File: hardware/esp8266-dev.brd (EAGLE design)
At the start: 48.3 x 48.3 mm, 19 parts, among them CON1 USBB-SOCKET, IC1 TBD, J1 AVR_SPI_PRG_6PTH

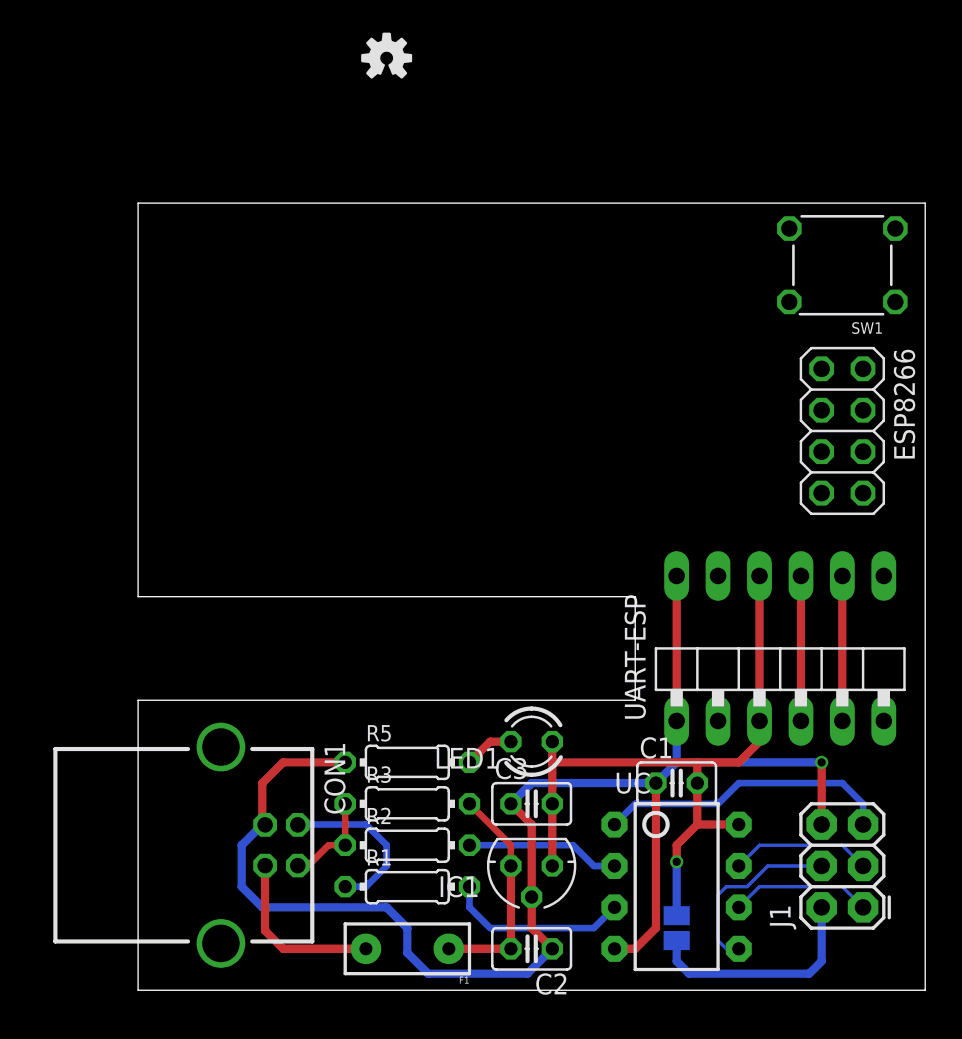
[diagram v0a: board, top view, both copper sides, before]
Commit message: Added ESP sub board with proto area
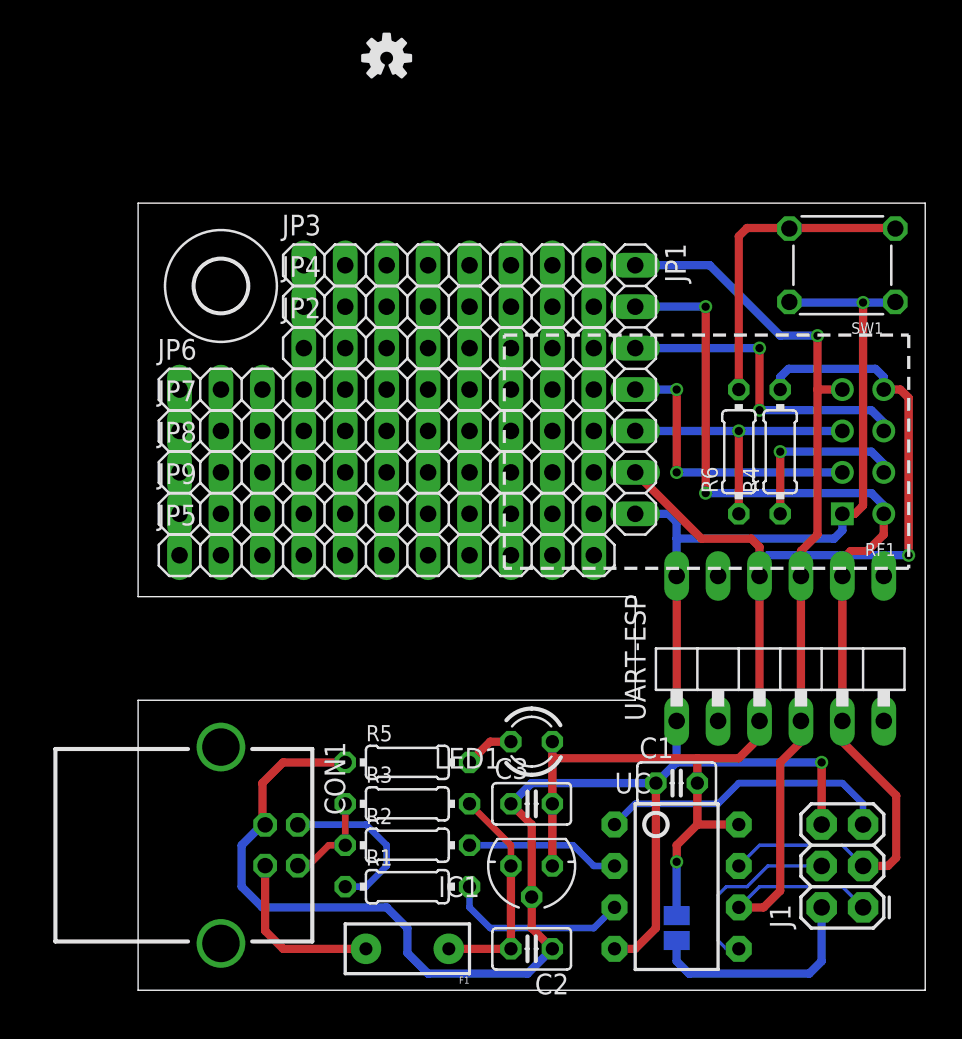
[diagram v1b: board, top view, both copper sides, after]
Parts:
- removed ESP8266: (no value), pinhead:2X04
- added H1: MOUNT-HOLE3.2, holes:3,2
- added JP1: (no value), pinhead:1X07
- added JP2, JP3, JP4: (no value), pinhead:1X08
- added JP5, JP6, JP7, JP8, JP9: (no value), pinhead:1X11
- added R4, R6: 10k, rcl:0204/7
- added RF1: ESP2866-ESP-01THT, p.peter-periphery:ESP8266-ESP-01
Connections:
- removed net N$7: UART-AVR.4, UART-ESP.4
- removed net PIN1: J1.1, UC.6
- removed net PIN2: J1.3, UC.7
- new net AVR-RX: J1.3, JP1.2, RF1.TX, UART-AVR.5, UART-ESP.5, UC.7
- new net AVR-TX: J1.1, JP1.1, RF1.RX, UART-AVR.4, UART-ESP.4, UC.6
- new net IO0: JP1.5, R6.1, RF1.GPIO0
- new net IO16: JP1.3, RF1.GPIO16
- new net IO2: JP1.4, RF1.GPIO2
- new net N$8: R6.2, SW1.P$1, SW1.P$2
- net +3V3: now also JP1.6, R4.2, RF1.VCC
- net GND: now also JP1.7, RF1.GND, SW1.P$3, SW1.P$4
- net N$6: now also R4.1, RF1.H_PD; no longer UART-AVR.5, UART-ESP.5
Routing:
- net AVR-RX: track 0.00 -> 62.5 mm, vias 0 -> 2
- net AVR-TX: track 0.00 -> 61.1 mm, vias 0 -> 1
- net +3V3: track 43.5 -> 84.6 mm, vias 1 -> 2
- net GND: track 92.8 -> 130.8 mm, vias 1 -> 2
- net IO16: track 0.00 -> 19.9 mm, vias 0 -> 2
- net N$8: track 0.00 -> 19.3 mm
- net IO0: track 0.00 -> 17.8 mm, vias 0 -> 1
- net IO2: track 0.00 -> 17.8 mm, vias 0 -> 2
- net N$7: track 8.89 -> 0.00 mm
- net PIN1: track 8.67 -> 0.00 mm
- net PIN2: track 8.67 -> 0.00 mm
- net N$6: track 8.89 -> 11.0 mm, vias 0 -> 1

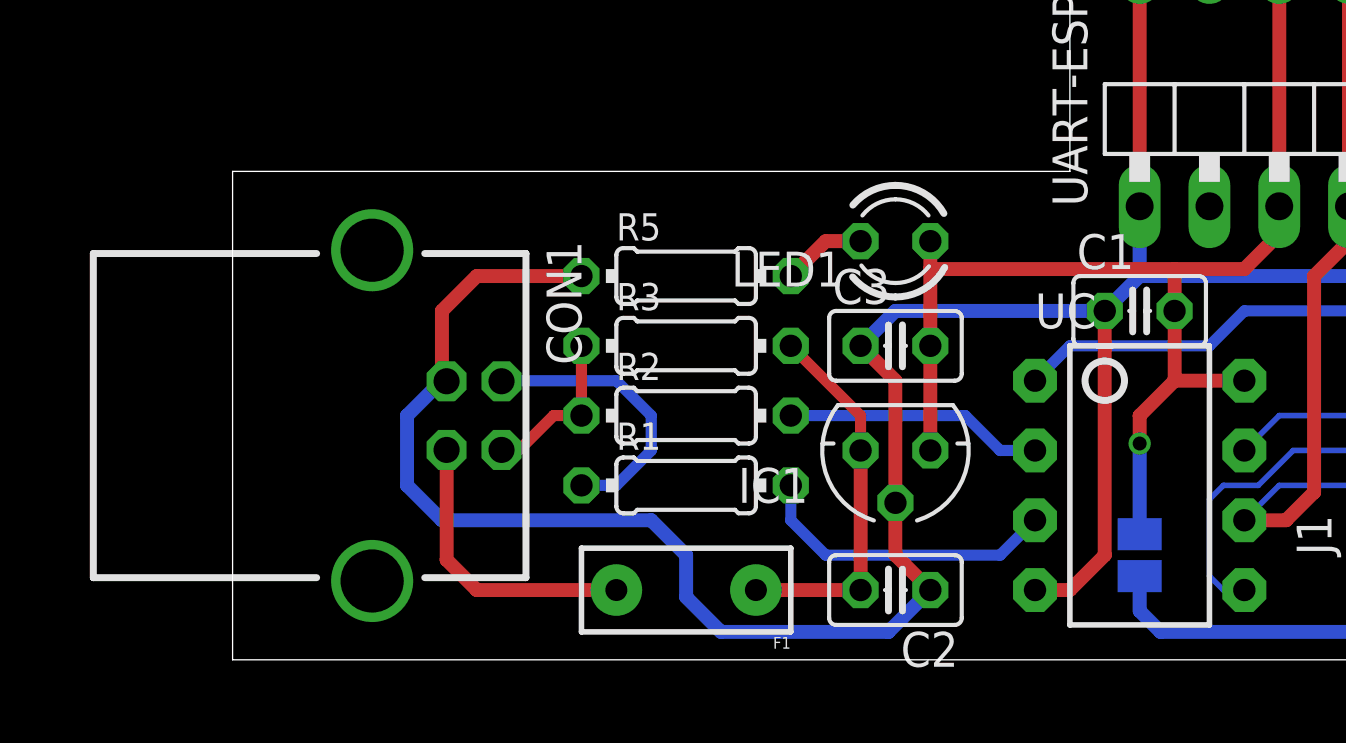
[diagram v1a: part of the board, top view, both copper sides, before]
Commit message: changed regulator to 500m suitable version and fuse to smaller footprint
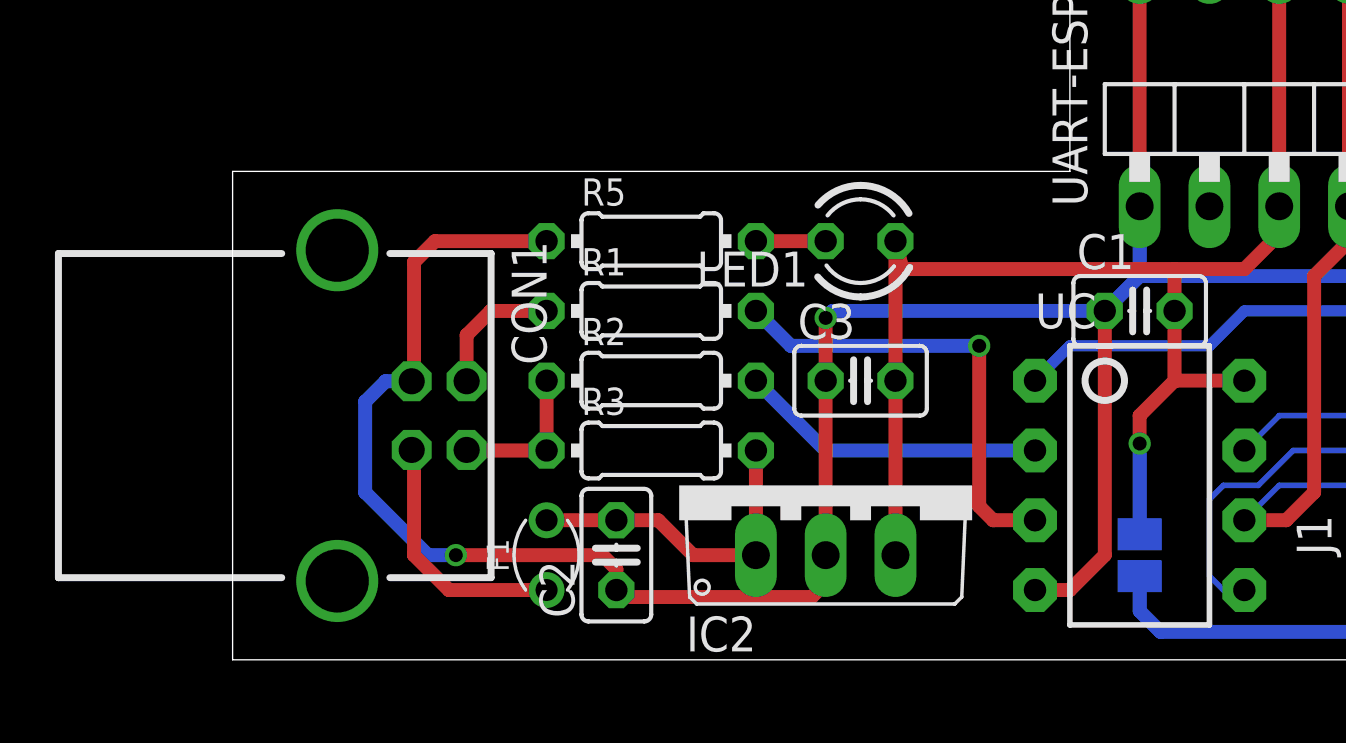
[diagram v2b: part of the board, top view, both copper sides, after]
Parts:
- removed IC1: TBD, v-reg:78LXX
- added IC2: (no value), p.peter-regulators:TO220V
- C2: value 100n -> 330n
- F1: value PTCPTH -> 500m; device SparkFun:PTC -> p.peter-regulators:FUSE-THT-100-MIL
- moved C2 10.2 mm to (14.0, 5.08), turned to 90 degrees
- moved R1 6.48 mm to (15.2, 14.0)
- moved F1 5.24 mm to (11.4, 5.08), turned to 90 degrees
- moved R3 4.02 mm to (15.2, 8.89)
- moved R5 1.80 mm to (15.2, 16.5)
- moved R2 1.80 mm to (15.2, 11.4)
- moved C3 1.80 mm to (22.9, 11.4)
- moved CON1 1.27 mm to (3.81, 10.2)
- moved LED1 1.27 mm to (22.9, 16.5)
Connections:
- net +3V3: now also IC2.3; no longer IC1.OUT
- net +5V: now also F1.P$2, IC2.1; no longer F1.P$1, IC1.IN
- net GND: now also IC2.2; no longer IC1.GND
- net N$4: now also F1.P$1; no longer F1.P$2
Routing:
- net +3V3: track 84.6 -> 90.4 mm
- net N$2: track 11.2 -> 16.7 mm, vias 0 -> 1
- net D+: track 10.4 -> 4.96 mm
- net N$1: track 9.42 -> 11.2 mm
- net +5V: track 13.8 -> 12.0 mm
- net N$4: track 10.6 -> 9.25 mm
- net GND: track 130.8 -> 129.6 mm, vias 2 -> 4
- net N$3: track 3.07 -> 2.54 mm

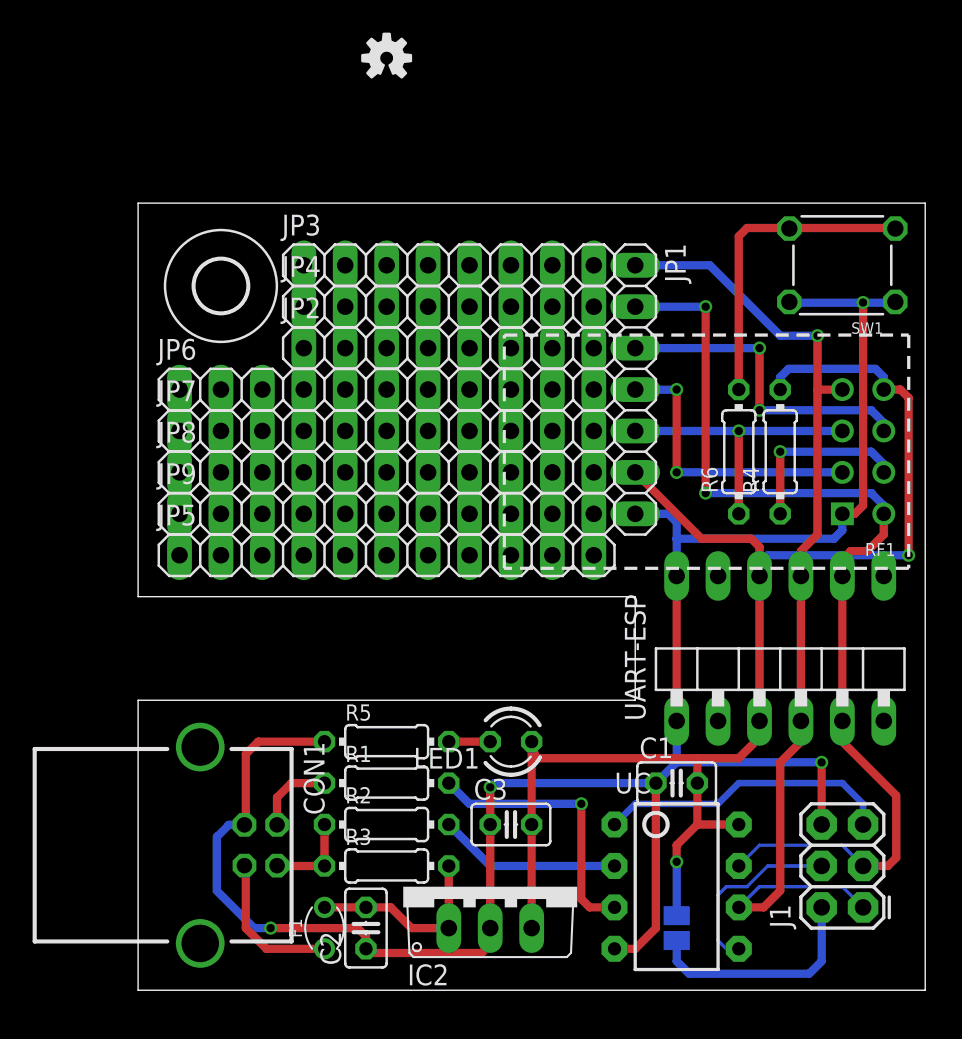
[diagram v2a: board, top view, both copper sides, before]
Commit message: basic lazyout done, cleaning up silkscreen
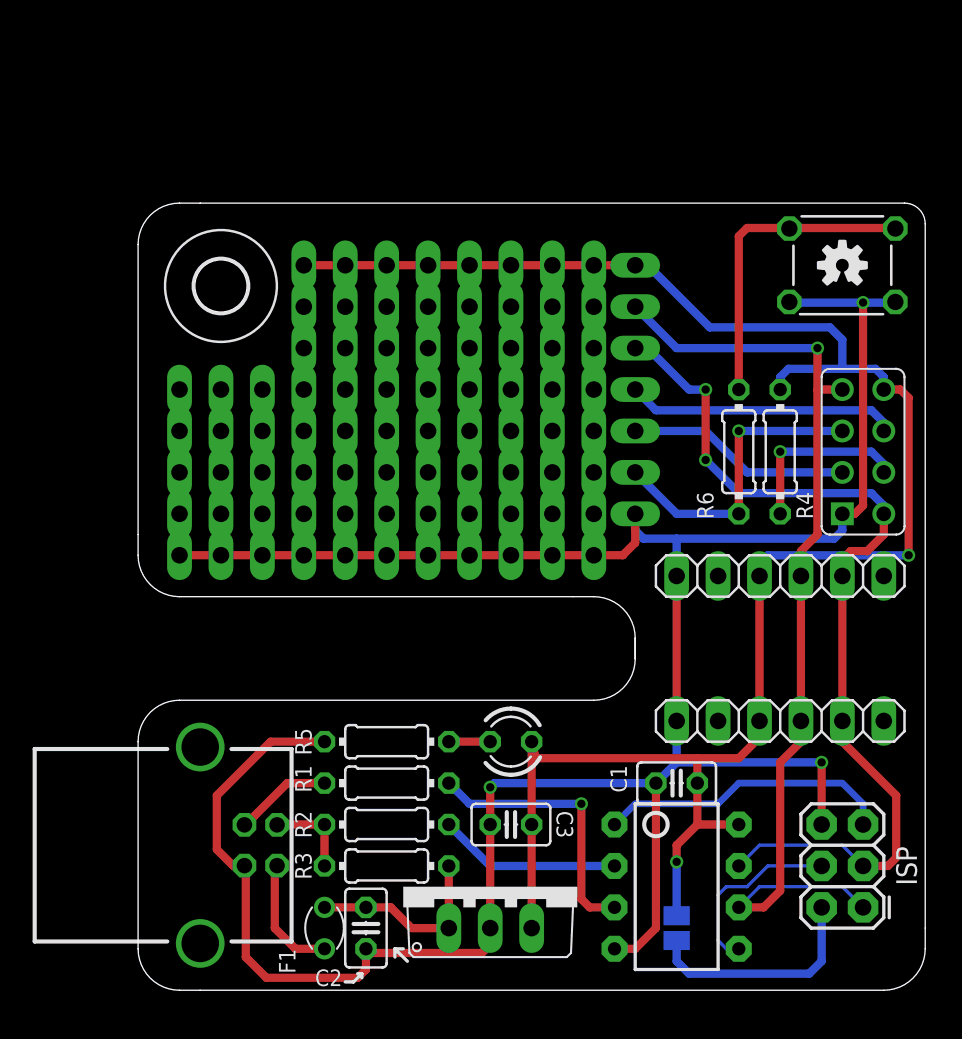
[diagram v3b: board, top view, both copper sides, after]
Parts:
- removed JP1: (no value), pinhead:1X07
- removed JP2, JP3, JP4: (no value), pinhead:1X08
- removed JP5, JP6, JP7, JP8, JP9: (no value), pinhead:1X11
- removed UART-AVR, UART-ESP: UART-6_PIN, p.peter-connectors:ANGLE-1X6
- added AVR-UART, ESP-UART: (no value), p.peter-connectors:PINHEADER-100MIL-1X6
- added CON10: (no value), p.peter-connectors:PINHEADER-100MIL-1X7-NOSILK
- added CON2, CON3, CON4: (no value), p.peter-connectors:PINHEADER-100MIL-1X8-NOSILK
- added CON5, CON6, CON7, CON8, CON9: (no value), p.peter-connectors:PINHEADER-100MIL-1X11-NOSILK
- RF1: value ESP2866-ESP-01THT -> (none); device p.peter-periphery:ESP8266-ESP-01 -> p.peter-periphery:ESP8266-ESP-01-NOSILK
- UC: value ATTINY45DIP8 -> ATTINY85
- moved U$1 30.7 mm to (43.2, 45.7)
- renumbered J1 to ISP
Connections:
- removed net N$5: CON1.D-, R2.1, R3.1
- new net D-: CON1.2, R2.1, R3.1
- net +3V3: now also AVR-UART.3, CON10.1, CON2.1, CON2.2, CON2.3, CON2.4, CON2.5, CON2.6, CON2.7, CON2.8, ESP-UART.3; no longer JP1.6, UART-AVR.3, UART-ESP.3
- net AVR-RX: now also AVR-UART.5, CON10.3, ESP-UART.5; no longer JP1.2, UART-AVR.5, UART-ESP.5
- net AVR-TX: now also AVR-UART.4, CON10.2, ESP-UART.4; no longer JP1.1, UART-AVR.4, UART-ESP.4
- net D+: now also CON1.3; no longer CON1.D+
- net GND: now also AVR-UART.1, CON1.4, CON10.7, CON5.1, CON5.10, CON5.11, CON5.2, CON5.3, CON5.4, CON5.5, CON5.6, CON5.7, CON5.8, CON5.9, ESP-UART.1; no longer CON1.GND, JP1.7, UART-AVR.1, UART-ESP.1
- net IO0: now also CON10.6; no longer JP1.5
- net IO16: now also CON10.4; no longer JP1.3
- net IO2: now also CON10.5; no longer JP1.4
- net N$4: now also CON1.1; no longer CON1.VUSB
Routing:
- net GND: track 129.6 -> 162.5 mm, vias 4 -> 3
- net +3V3: track 90.4 -> 115.8 mm
- net N$5: track 5.73 -> 0.00 mm
- net D-: track 0.00 -> 5.45 mm
- net AVR-RX: track 62.5 -> 57.3 mm
- net IO2: track 17.8 -> 13.8 mm, vias 2 -> 0
- net IO16: track 19.9 -> 16.6 mm, vias 2 -> 0
- net N$4: track 9.25 -> 7.52 mm
- net AVR-TX: track 61.1 -> 59.6 mm
- net IO0: track 17.8 -> 18.8 mm
- net D+: track 4.96 -> 5.95 mm
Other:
- outline, holes or cut-outs redrawn
